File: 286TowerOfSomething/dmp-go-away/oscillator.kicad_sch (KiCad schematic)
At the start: 1 part, among them U1 M6117C

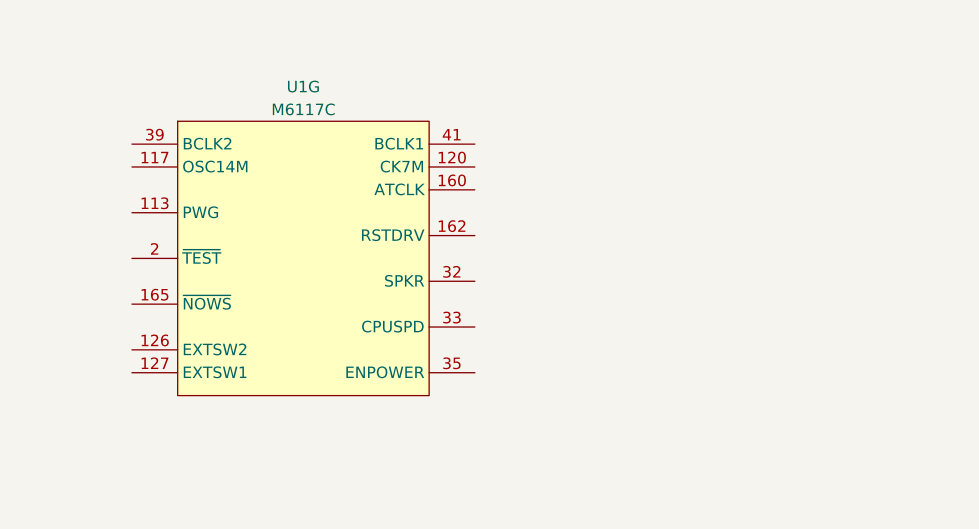
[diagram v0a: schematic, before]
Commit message: Adding work done on 386 card, coming along nicely
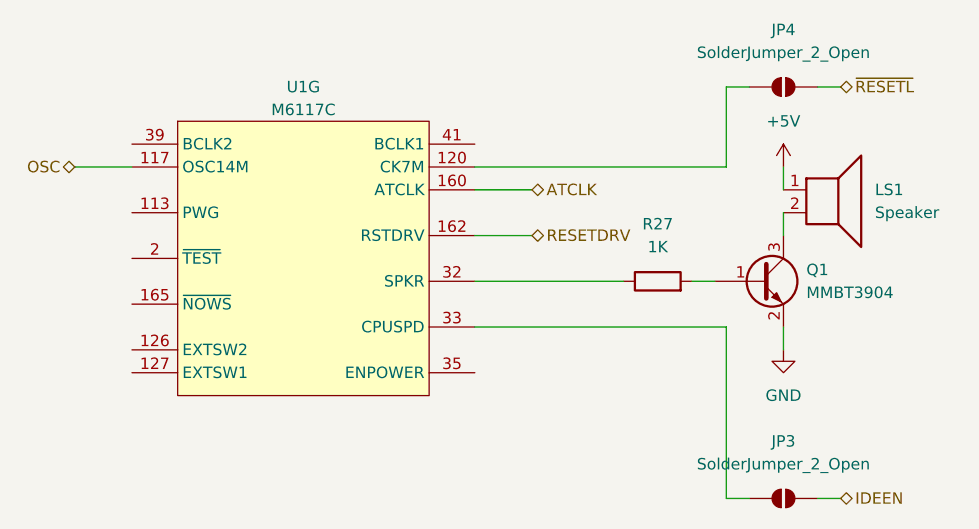
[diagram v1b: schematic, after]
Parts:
- added JP3, JP4: SolderJumper_2_Open, symbol Jumper:SolderJumper_2_Open
- added LS1: Speaker, symbol Device:Speaker
- added Q1: MMBT3904, Package_TO_SOT_SMD:SOT-23, symbol Transistor_BJT:MMBT3904
- added R27: 1K, symbol Device:R
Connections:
- net OSC: now reaches U1.117 (OSC14M)
- net at U1.120 (CK7M): now also JP4.1 (A)
- net ATCLK: now reaches U1.160 (ATCLK)
- net RESETDRV: now reaches U1.162 (RSTDRV)
- net at U1.32 (SPKR): now also R27.1
- net at U1.33 (CPUSPD): now also JP3.1 (A)
- new net: Q1.1 (B), R27.2
- new net: LS1.2, Q1.3 (C)
- new net +5V: LS1.1
- new net GND: Q1.2 (E)
- new net IDEEN: JP3.2 (B)
- new net ~{RESETL}: JP4.2 (B)

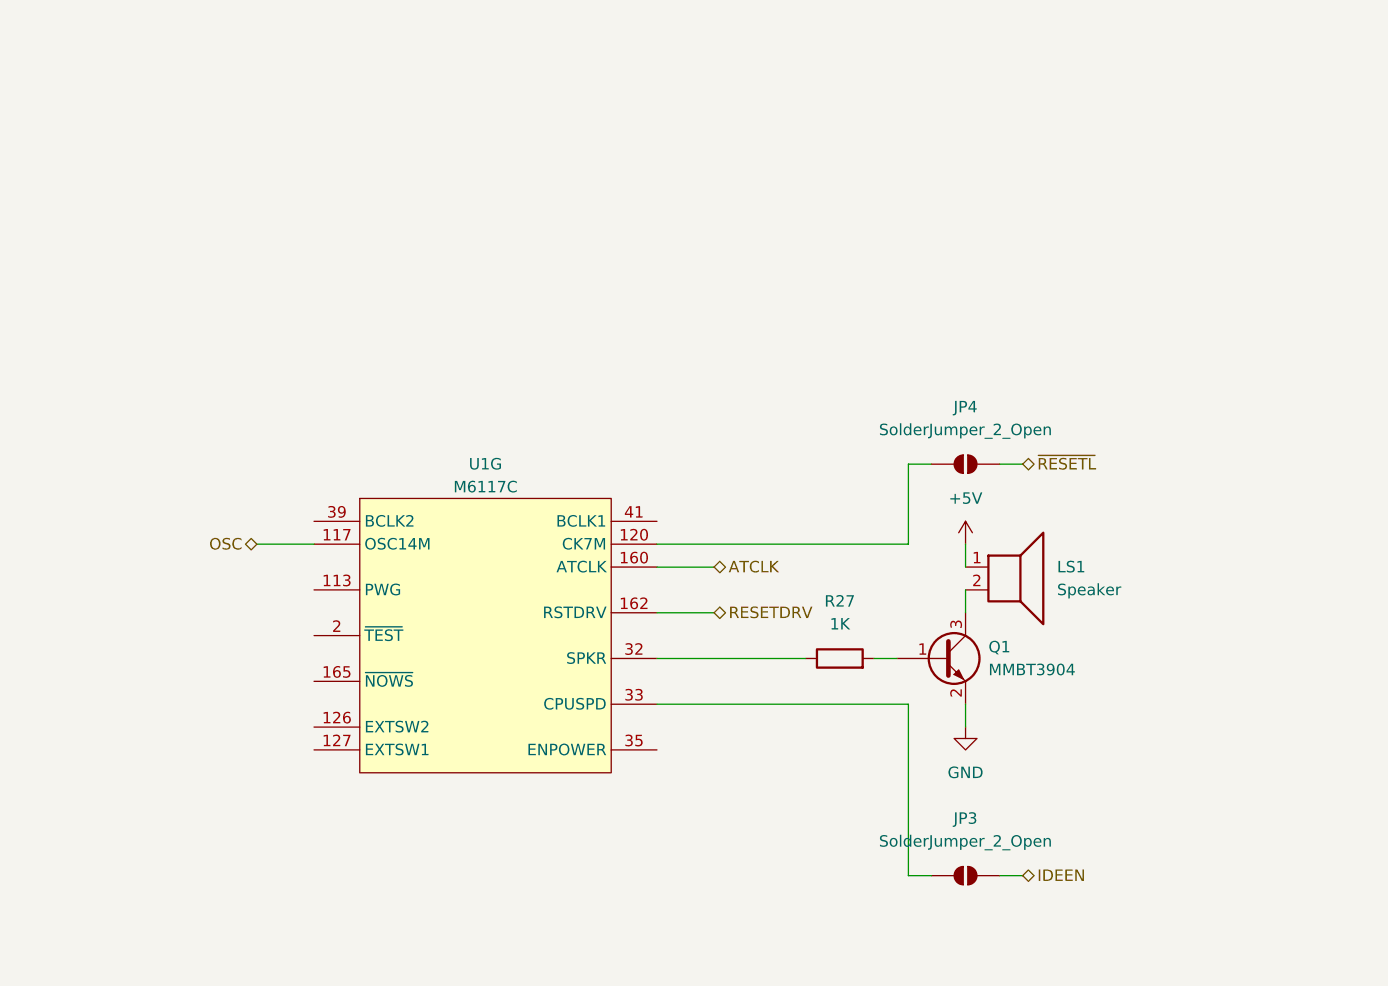
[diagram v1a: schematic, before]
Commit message: Adding keyboard/mouse and oscillator to schematic of dmp-go-away
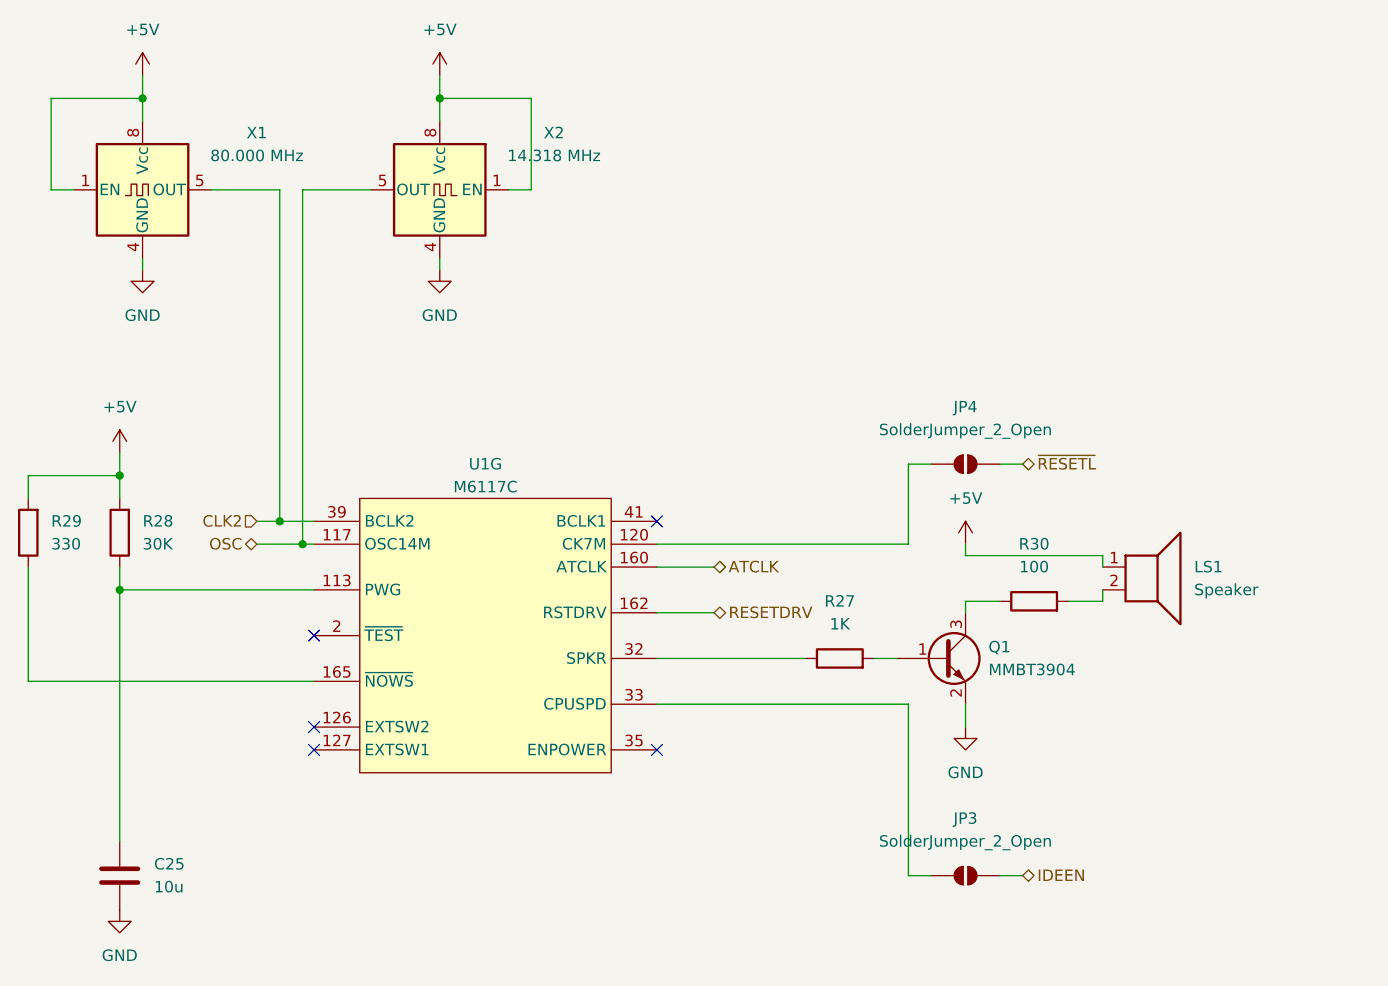
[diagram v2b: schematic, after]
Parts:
- added C25: 10u, symbol Device:C
- added R28: 30K, symbol Device:R
- added R29: 330, symbol Device:R
- added R30: 100, symbol Device:R
- added X1: 80.000 MHz, Oscillator:Oscillator_DIP-8, symbol Oscillator:CXO_DIP8
- added X2: 14.318 MHz, Oscillator:Oscillator_DIP-8, symbol Oscillator:CXO_DIP8
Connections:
- net +5V: now also R28.2, R29.2, X1.1 (EN), X1.8 (Vcc), X2.1 (EN), X2.8 (Vcc)
- net GND: now also C25.2, X1.4 (GND), X2.4 (GND)
- net OSC: now also X2.5 (OUT)
- net at U1.113 (PWG): now also C25.1, R28.1
- net at U1.165 (~{NOWS}): now also R29.1
- net CLK2: now reaches U1.39 (BCLK2)
- net CLK2: now also X1.5 (OUT)
- net at Q1.3 (C): now also R30.1; no longer LS1.2
- new net: LS1.2, R30.2
- no-connect marks 0 -> 5
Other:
- moved on the sheet: LS1

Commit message: Adding some missing caps, and the optional DS12885 RTC for dmp-go-away
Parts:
- added C32, C33: 100n, symbol Device:C
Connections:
- net +5V: now also C32.1, C33.1
- net GND: now also C32.2, C33.2

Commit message: Added footprints and started figuring out layout for dmp-go-away
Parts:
- C25: footprint (none) -> Capacitor_SMD:C_1206_3216Metric_Pad1.33x1.80mm_HandSolder
- C32, C33: footprint (none) -> Capacitor_SMD:C_0603_1608Metric_Pad1.08x0.95mm_HandSolder
- JP3, JP4: footprint (none) -> Jumper:SolderJumper-2_P1.3mm_Open_RoundedPad1.0x1.5mm
- LS1: footprint (none) -> Buzzer_Beeper:Buzzer_TDK_PS1240P02BT_D12.2mm_H6.5mm
- R27, R28, R29, R30: footprint (none) -> Resistor_SMD:R_0603_1608Metric_Pad0.98x0.95mm_HandSolder
- U1: footprint (none) -> Package_QFP:PQFP-208_28x28mm_P0.5mm
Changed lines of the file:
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@@
 			)
 		)
-		(property "Footprint" ""
+		(property "Footprint" "Capacitor_SMD:C_0603_1608Metric_Pad1.08x0.95mm_HandSolder"
 			(at 166.0652 54.61 0)
 			(effects
@@
 			)
 		)
-		(property "Footprint" ""
+		(property "Footprint" "Resistor_SMD:R_0603_1608Metric_Pad0.98x0.95mm_HandSolder"
 			(at 37.338 88.9 90)
 			(effects
@@
 			)
 		)
-		(property "Footprint" ""
+		(property "Footprint" "Package_QFP:PQFP-208_28x28mm_P0.5mm"
 			(at 76.2 100.33 0)
 			(effects
@@
 			)
 		)
-		(property "Footprint" ""
+		(property "Footprint" "Resistor_SMD:R_0603_1608Metric_Pad0.98x0.95mm_HandSolder"
 			(at 115.57 104.648 90)
 			(effects
@@
 			)
 		)
-		(property "Footprint" ""
+		(property "Footprint" "Capacitor_SMD:C_1206_3216Metric_Pad1.33x1.80mm_HandSolder"
 			(at 36.5252 130.81 0)
 			(effects
@@
 			)
 		)
-		(property "Footprint" ""
+		(property "Footprint" "Capacitor_SMD:C_0603_1608Metric_Pad1.08x0.95mm_HandSolder"
 			(at 153.3652 54.61 0)
 			(effects
@@
 			)
 		)
-		(property "Footprint" ""
+		(property "Footprint" "Resistor_SMD:R_0603_1608Metric_Pad0.98x0.95mm_HandSolder"
 			(at 27.178 88.9 90)
 			(effects
@@
 			)
 		)
-		(property "Footprint" ""
+		(property "Footprint" "Jumper:SolderJumper-2_P1.3mm_Open_RoundedPad1.0x1.5mm"
 			(at 129.54 127 0)
 			(effects
@@
 			)
 		)
-		(property "Footprint" ""
+		(property "Footprint" "Resistor_SMD:R_0603_1608Metric_Pad0.98x0.95mm_HandSolder"
 			(at 137.16 98.298 90)
 			(effects
@@
 			)
 		)
-		(property "Footprint" ""
+		(property "Footprint" "Jumper:SolderJumper-2_P1.3mm_Open_RoundedPad1.0x1.5mm"
 			(at 129.54 81.28 0)
 			(effects
@@
 			)
 		)
-		(property "Footprint" ""
+		(property "Footprint" "Buzzer_Beeper:Buzzer_TDK_PS1240P02BT_D12.2mm_H6.5mm"
 			(at 149.86 97.79 0)
 			(effects
